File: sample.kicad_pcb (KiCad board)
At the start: 2 copper layers, 35 parts, among them CN10 Conn_02x17_Odd_Even, CN7 Conn_02x10_Odd_Even, CN8 Conn_02x08_Odd_Even, CN9 Conn_02x15_Odd_Even, U1 TJA1042T-3, U2 TJA1042T-3, U3 TJA1042T-3

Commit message: placements
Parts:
- moved U1 1.24 mm to (128.3, 57.7)
- moved U2 0.87 mm to (128.3, 89.7)
- moved CAN1 0.74 mm to (163.3, 53.0)
- moved U3 0.37 mm to (128.3, 117.7)
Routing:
- net CAN1_H: track 0.00 -> 35.1 mm
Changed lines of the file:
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@@
 	(footprint "Package_SO:SOIC-8_3.9x4.9mm_P1.27mm"
 		(layer "F.Cu")
-		(at 127.4 89.74)
+		(at 128.27 89.74)
 		(descr "SOIC, 8 Pin (JEDEC MS-012AA, https://www.analog.com/media/en/package-pcb-resources/package/pkg_pdf/soic_narrow-r/r_8.pdf), generated with kicad-footprint-generator ipc_gullwing_generator.py")
 		(tags "SOIC SO")
@@
 	(footprint "Package_SO:SOIC-8_3.9x4.9mm_P1.27mm"
 		(layer "F.Cu")
-		(at 127.9 117.74)
+		(at 128.27 117.74)
 		(descr "SOIC, 8 Pin (JEDEC MS-012AA, https://www.analog.com/media/en/package-pcb-resources/package/pkg_pdf/soic_narrow-r/r_8.pdf), generated with kicad-footprint-generator ipc_gullwing_generator.py")
 		(tags "SOIC SO")
@@
 	(footprint "Connector_Dsub:DSUB-9_Female_Horizontal_P2.77x2.54mm_EdgePinOffset9.40mm"
 		(layer "F.Cu")
-		(at 163.269669 53.69 90)
+		(at 163.269669 52.95 90)
 		(descr "9-pin D-Sub connector, horizontal/angled (90 deg), THT-mount, female, pitch 2.77x2.54mm, pin-PCB-offset 9.4mm, see http://docs-europe.electrocomponents.com/webdocs/1585/0900766b81585df2.pdf")
 		(tags "9-pin D-Sub connector horizontal angled 90deg THT female pitch 2.77x2.54mm pin-PCB-offset 9.4mm")
@@
 	(footprint "Package_SO:SOIC-8_3.9x4.9mm_P1.27mm"
 		(layer "F.Cu")
-		(at 129.4 58.24)
+		(at 128.27 57.74)
 		(descr "SOIC, 8 Pin (JEDEC MS-012AA, https://www.analog.com/media/en/package-pcb-resources/package/pkg_pdf/soic_narrow-r/r_8.pdf), generated with kicad-footprint-generator ipc_gullwing_generator.py")
 		(tags "SOIC SO")
@@
 	)
 	(gr_line
-		(start 98.9 126.74)
-		(end 178.401667 126.74)
-		(stroke
-			(width 0.1)
-			(type default)
-		)
-		(layer "F.SilkS")
-	)
-	(gr_line
 		(start 103.4 126.74)
 		(end 103.4 94.74)
@@
 		(layer "F.SilkS")
 	)
+	(segment
+		(start 130.745 57.105)
+		(end 165.809669 57.105)
+		(width 0.2)
+		(layer "F.Cu")
+		(net 19)
+	)
 )

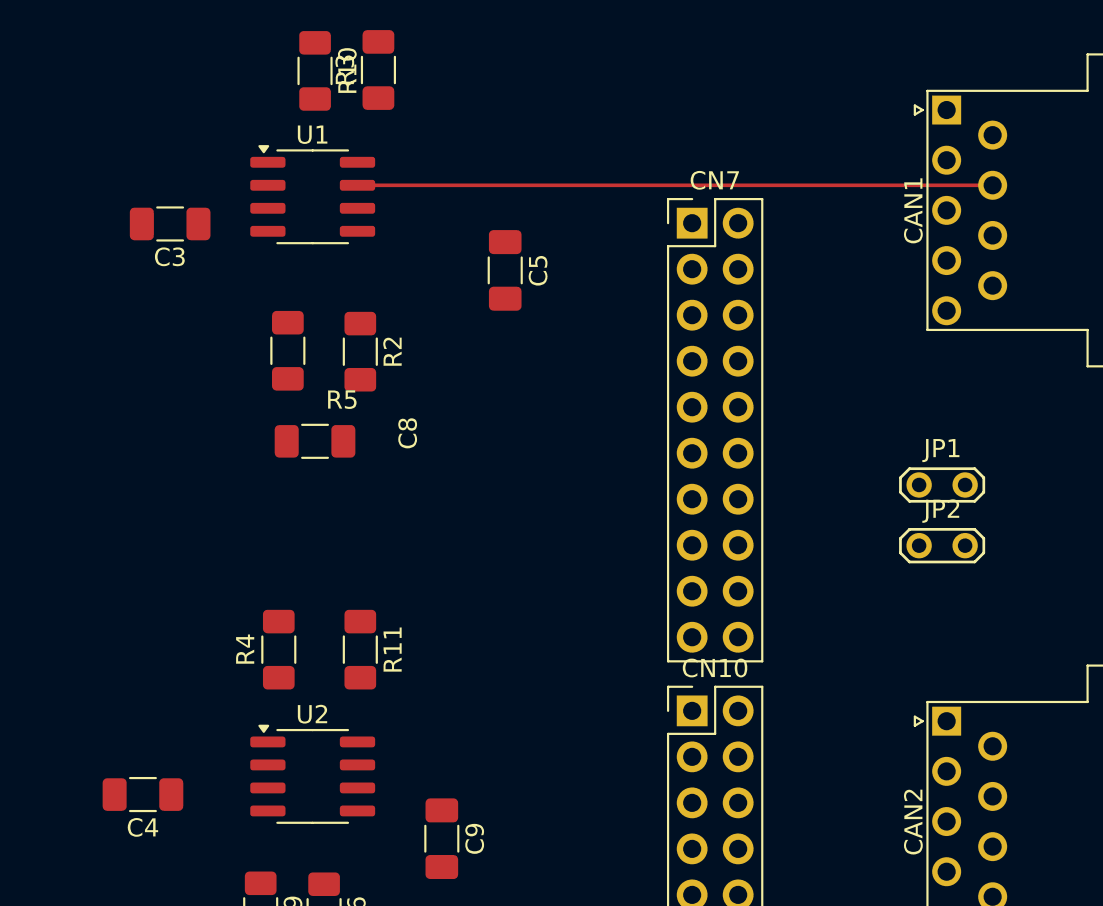
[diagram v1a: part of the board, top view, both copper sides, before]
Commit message: adapt Signal net rule
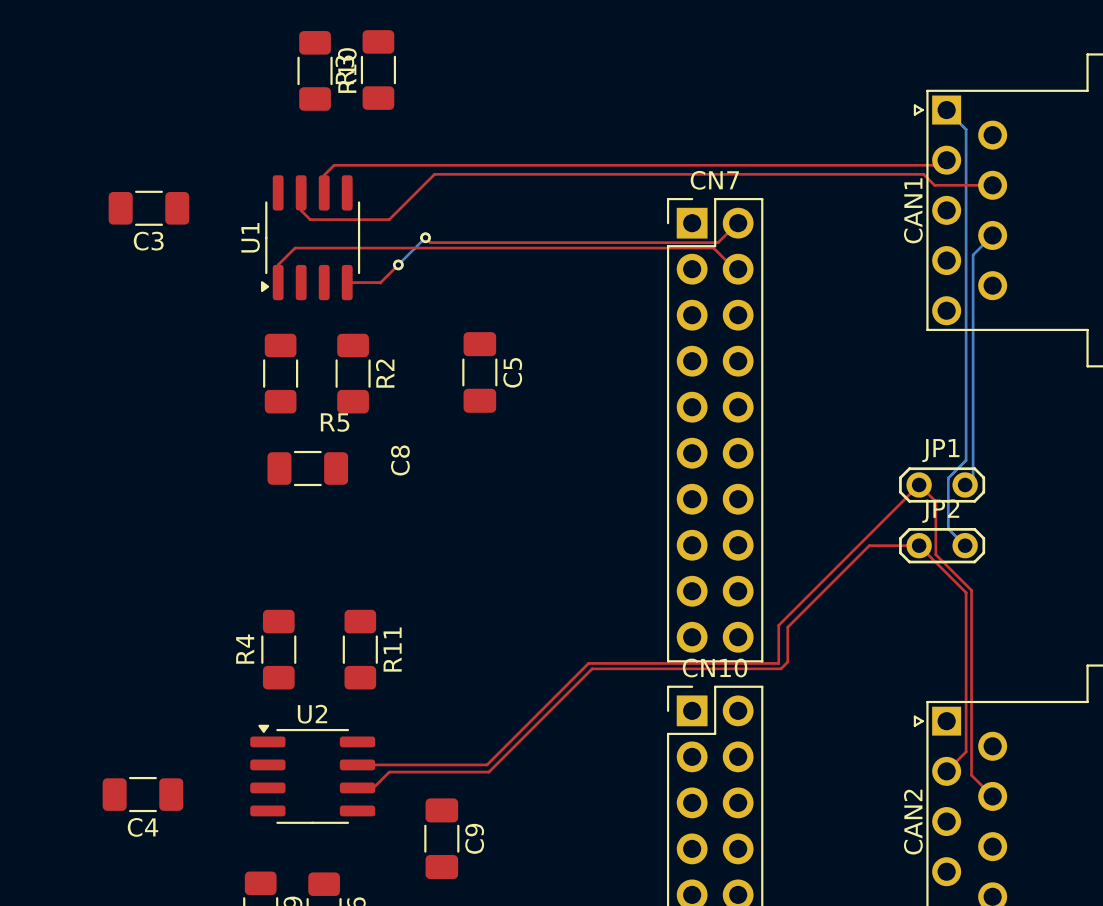
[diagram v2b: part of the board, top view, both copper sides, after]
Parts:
- moved C5 5.81 mm to (137.5, 67.4)
- moved U1 2.26 mm to (128.3, 60.0), turned to 90 degrees
- moved C8 1.55 mm to (128.0, 72.7)
- moved C3 1.45 mm to (119.2, 58.4)
- moved R5 1.32 mm to (126.5, 67.5)
- moved R2 1.27 mm to (130.5, 67.5)
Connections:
- net Net-(JP1-B) renamed CAN2_HR
- net Net-(JP2-B) renamed CAN2_LR
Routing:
- net CAN2_H: track 0.00 -> 57.5 mm
- net CAN2_L: track 0.00 -> 51.7 mm
- net CAN1_L: track 0.00 -> 35.7 mm
- net CAN1_TX: track 0.00 -> 27.0 mm
- net CAN2_LR: track 0.00 -> 25.3 mm
- net CAN1_RX: track 0.00 -> 23.2 mm, vias 0 -> 2
- net CAN2_HR: track 0.00 -> 14.4 mm
- net CAN1_H: track 35.1 -> 40.6 mm

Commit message: uarts routed
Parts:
- moved C2 14.1 mm to (121.5, 123.5)
- moved C1 3.42 mm to (121.0, 115.5)
- moved R12 1.42 mm to (125.0, 109.5)
- moved R1 0.90 mm to (129.5, 109.7)
- turned U3 to -90 degrees
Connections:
- CN10 pad 2: USART10_TX -> /ZIO Connector/PG12
- CN10 pad 25: USART10_RX -> unconnected-(CN10-Pin_25-Pad25)
- CN10 pad 28: /ZIO Connector/PE6 -> unconnected-(CN10-Pin_28-Pad28)
- CN10 pad 29: UART4_TX -> /ZIO Connector/PA0
- CN8 pad 8: UART4_RX -> /ZIO Connector/PC11
- CN9 pad 22: /ZIO Connector/PE3 -> USART10_TX
- CN9 pad 25: /ZIO Connector/PD0 -> UART4_RX
- CN9 pad 27: /ZIO Connector/PD1 -> UART4_TX
- DeviceUART1 pad 1: USART2_TX -> UART7_TX
- DeviceUART1 pad 4: USART6_RX -> UART9_RX
- DeviceUART1 pad 5: USART10_RX -> UART4_RX
- DeviceUART1 pad 6: USART2_RX -> UART7_RX
- DeviceUART1 pad 8: USART6_TX -> UART9_TX
- DeviceUART1 pad 9: USART10_TX -> UART4_TX
- RoutedUART1 pad 1: UART4_RX -> USART6_RX
- RoutedUART1 pad 4: UART7_TX -> USART2_TX
- RoutedUART1 pad 5: UART9_TX -> USART10_TX
- RoutedUART1 pad 6: UART4_TX -> USART6_TX
- RoutedUART1 pad 8: UART7_RX -> USART2_RX
- RoutedUART1 pad 9: UART9_RX -> USART10_RX
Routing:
- net UART7_RX: track 0.00 -> 103.8 mm
- net UART7_TX: track 0.00 -> 102.1 mm
- net USART6_RX: track 0.00 -> 85.5 mm
- net USART3_RX: track 0.00 -> 81.6 mm
- net USART3_TX: track 0.00 -> 78.9 mm
- net USART6_TX: track 0.00 -> 78.1 mm
- net USART10_TX: track 0.00 -> 44.0 mm
- net CAN3_H: track 0.00 -> 40.0 mm
- net CAN3_L: track 0.00 -> 38.9 mm
- net USART10_RX: track 0.00 -> 37.7 mm
- net CAN2_TX: track 0.00 -> 32.7 mm
- net CAN2_RX: track 0.00 -> 30.6 mm, vias 0 -> 2
- net UART9_TX: track 0.00 -> 27.8 mm
- net UART4_TX: track 0.00 -> 27.6 mm
- net USART2_TX: track 0.00 -> 26.2 mm
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
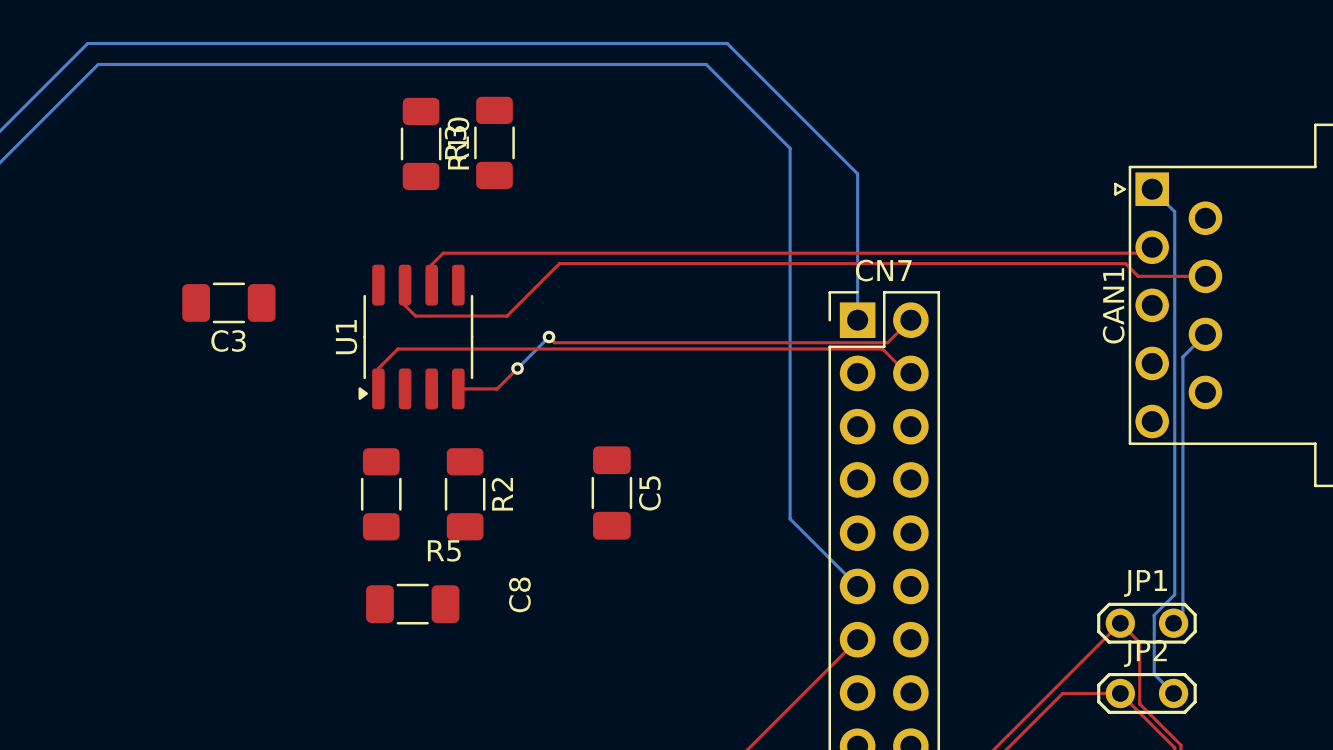
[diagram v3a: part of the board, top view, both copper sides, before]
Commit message: some connection for CAN1
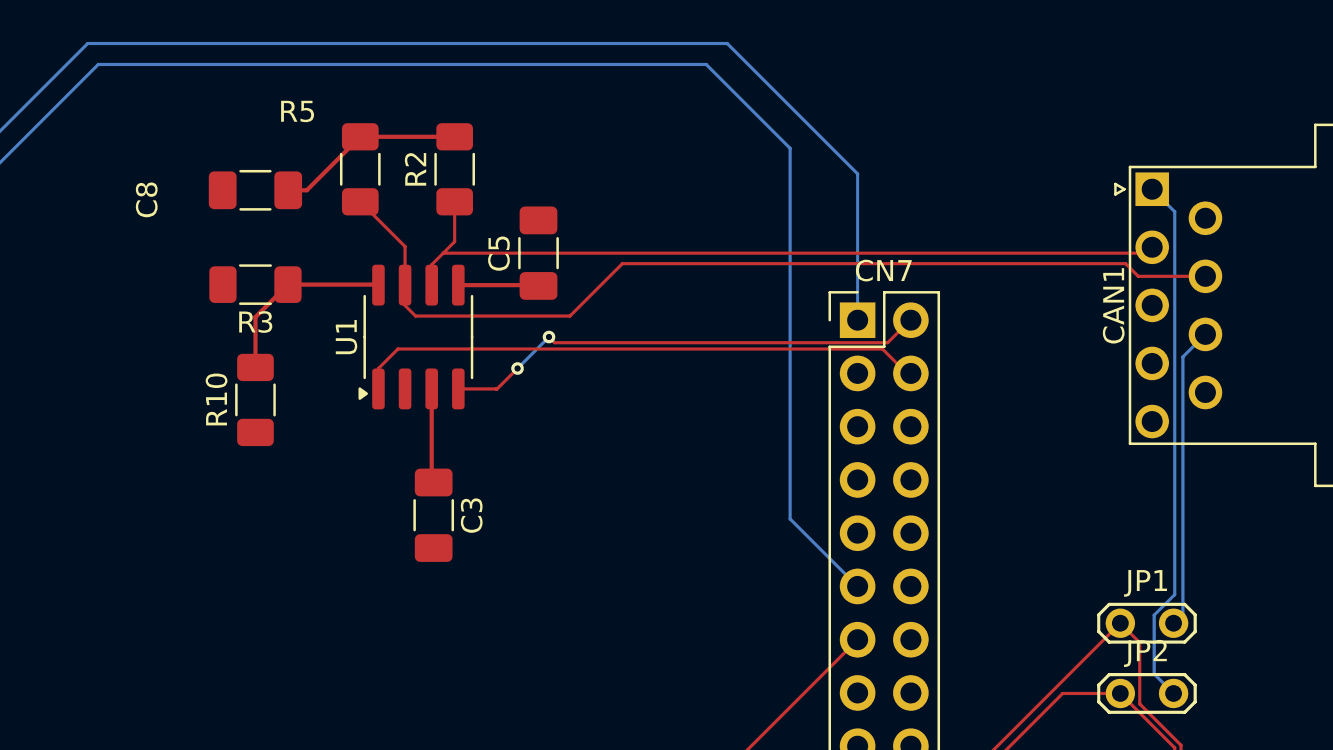
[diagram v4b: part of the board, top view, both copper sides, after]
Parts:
- moved C8 21.1 mm to (120.5, 53.0), turned to 180 degrees
- moved R5 15.5 mm to (125.5, 52.0), turned to 90 degrees
- moved R2 15.5 mm to (130.0, 52.0), turned to 90 degrees
- moved R10 14.5 mm to (120.5, 63.0), turned to 90 degrees
- moved C3 14.1 mm to (129.0, 68.5), turned to -90 degrees
- moved R3 13.3 mm to (120.5, 57.5), turned to 180 degrees
- moved C5 12.0 mm to (134.0, 56.0), turned to 90 degrees
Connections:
- CN7 pad 3: /ZIO Connector/PB15 -> CAN1_STB
- CN7 pad 7: CAN1_STB -> /ZIO Connector/PB12
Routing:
- net Net-(C8-Pad1): track 0.00 -> 8.99 mm
- net Net-(U1-STB): track 0.00 -> 8.92 mm
- net CAN1_H: track 40.6 -> 45.5 mm
- net +5V: track 0.00 -> 4.50 mm
- net +3V3: track 0.00 -> 3.89 mm
- net CAN1_L: track 35.7 -> 38.4 mm

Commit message: CAN1 finished
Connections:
- CN7 pad 14: CAN2_RX -> unconnected-(CN7-Pin_14-Pad14)
- CN7 pad 3: CAN1_STB -> /ZIO Connector/PB15
- CN7 pad 7: /ZIO Connector/PB12 -> CAN1_STB
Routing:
- net CAN1_STB: track 0.00 -> 29.7 mm, vias 0 -> 1
- net USART6_RX: track 85.5 -> 88.0 mm
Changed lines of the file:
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@@
 	(net 122 "unconnected-(CN10-Pin_28-Pad28)")
 	(net 123 "unconnected-(CN10-Pin_25-Pad25)")
-	(net 124 "/ZIO Connector/PB12")
+	(net 124 "/ZIO Connector/PB15")
+	(net 125 "unconnected-(CN7-Pin_14-Pad14)")
 	(footprint "Capacitor_SMD:C_1206_3216Metric_Pad1.33x1.80mm_HandSolder"
 		(layer "F.Cu")
@@
 			(layers "*.Cu" "*.Mask")
 			(remove_unused_layers no)
-			(net 17 "CAN1_STB")
+			(net 124 "/ZIO Connector/PB15")
 			(pinfunction "Pin_3")
 			(pintype "passive")
@@
 			(layers "*.Cu" "*.Mask")
 			(remove_unused_layers no)
-			(net 124 "/ZIO Connector/PB12")
+			(net 17 "CAN1_STB")
 			(pinfunction "Pin_7")
 			(pintype "passive")
@@
 			(layers "*.Cu" "*.Mask")
 			(remove_unused_layers no)
-			(net 25 "CAN2_RX")
+			(net 125 "unconnected-(CN7-Pin_14-Pad14)")
 			(pinfunction "Pin_14")
-			(pintype "passive")
+			(pintype "passive+no_connect")
 		)
 		(pad "15" thru_hole oval
@@
 	)
 	(segment
+		(start 120.5 64.55)
+		(end 122.45 64.55)
+		(width 0.15)
+		(layer "F.Cu")
+		(net 17)
+	)
+	(segment
+		(start 122.45 64.55)
+		(end 122.5 64.5)
+		(width 0.15)
+		(layer "F.Cu")
+		(net 17)
+	)
+	(via
+		(at 122.5 64.5)
+		(size 0.6)
+		(drill 0.3)
+		(layers "F.Cu" "B.Cu")
+		(net 17)
+	)
+	(segment
+		(start 122.5 64.5)
+		(end 146.904 64.5)
+		(width 0.15)
+		(layer "B.Cu")
+		(net 17)
+	)
+	(segment
+		(start 146.904 64.5)
+		(end 149.22 66.816)
+		(width 0.15)
+		(layer "B.Cu")
+		(net 17)
+	)
+	(segment
 		(start 162.605 57.105)
 		(end 165.809669 57.105)
@@
 	)
 	(segment
-		(start 93.930331 66.069669)
-		(end 93.930331 67.69)
+		(start 146.811 62.811)
+		(end 146 62)
 		(width 0.15)
 		(layer "B.Cu")
@@
 	)
 	(segment
-		(start 113 47)
-		(end 93.930331 66.069669)
+		(start 149.27528 62.811)
+		(end 150.5 64.03572)
 		(width 0.15)
 		(layer "B.Cu")
@@
 	)
 	(segment
-		(start 146 51)
-		(end 142 47)
+		(start 113 47)
+		(end 93.930331 66.069669)
 		(width 0.15)
 		(layer "B.Cu")
@@
 	(segment
 		(start 149.22 71.896)
-		(end 146 68.676)
+		(end 150.5 70.616)
 		(width 0.15)
 		(layer "B.Cu")
@@
 	)
 	(segment
-		(start 146 68.676)
+		(start 146 62)
 		(end 146 51)
 		(width 0.15)
@@
 	)
 	(segment
+		(start 146.811 62.811)
+		(end 149.27528 62.811)
+		(width 0.15)
+		(layer "B.Cu")
+		(net 98)
+	)
+	(segment
+		(start 93.930331 66.069669)
+		(end 93.930331 67.69)
+		(width 0.15)
+		(layer "B.Cu")
+		(net 98)
+	)
+	(segment
+		(start 150.5 70.616)
+		(end 150.5 64.03572)
+		(width 0.15)
+		(layer "B.Cu")
+		(net 98)
+	)
+	(segment
 		(start 142 47)
 		(end 113 47)
 		(width 0.15)
 		(layer "B.Cu")
+		(net 98)
+	)
+	(segment
+		(start 146 51)
+		(end 142 47)
+		(width 0.15)
+		(layer "B.Cu")

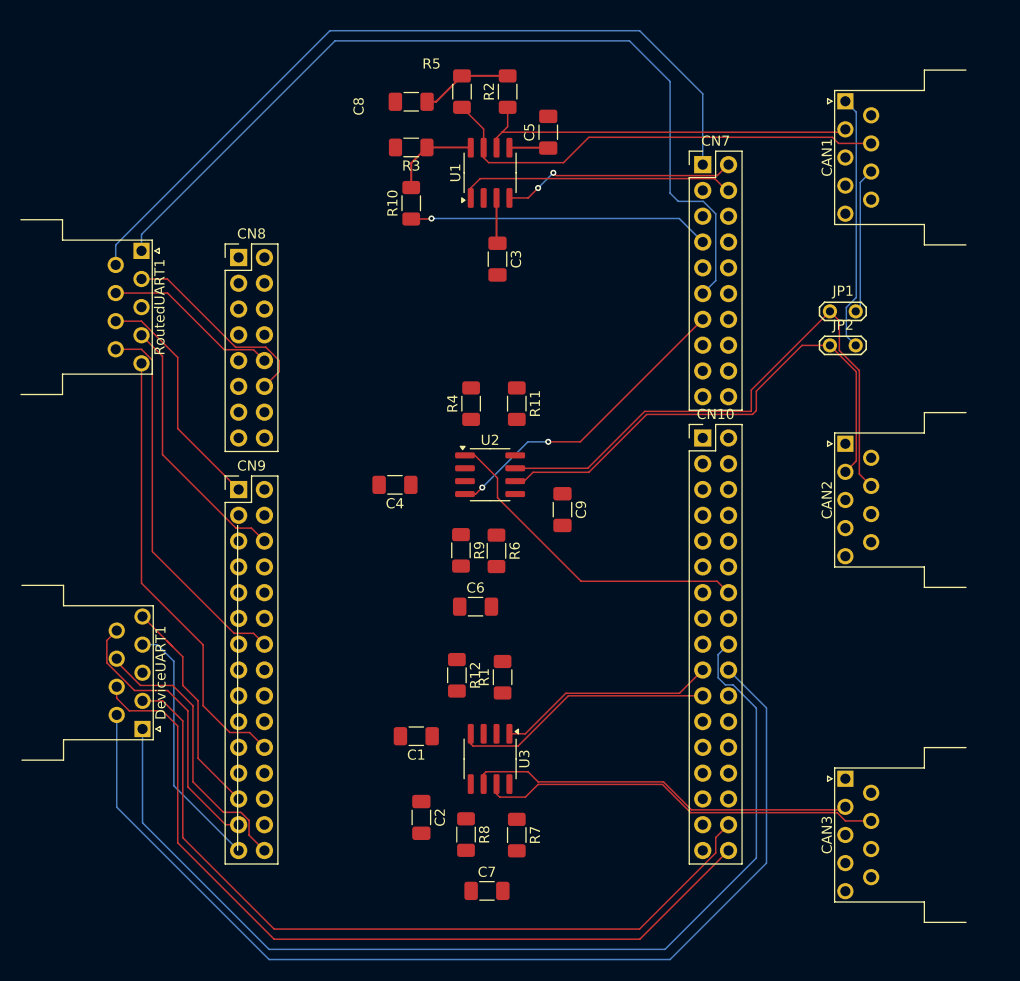
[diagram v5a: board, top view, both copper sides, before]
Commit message: All nets conected except GND, +3V3, +5V
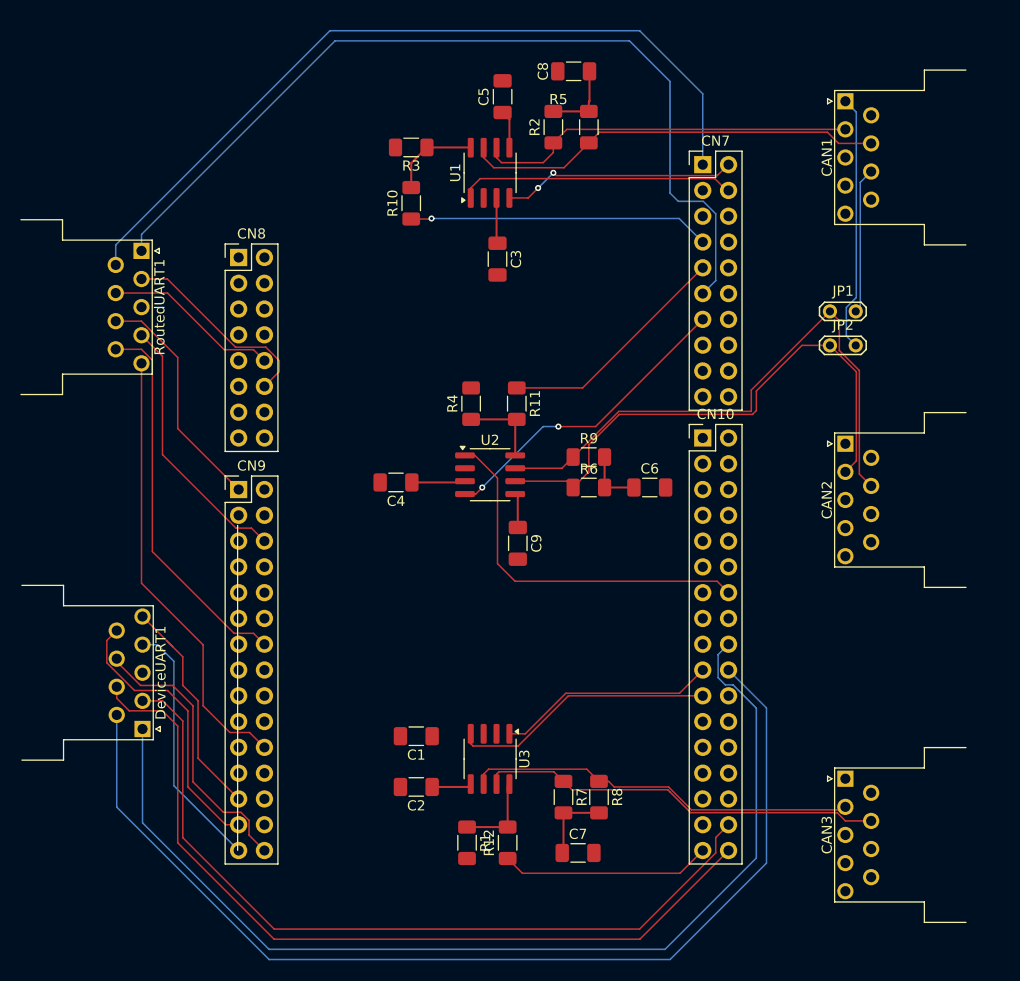
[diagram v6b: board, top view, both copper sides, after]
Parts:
- moved C6 20.8 mm to (144.0, 91.0)
- moved R12 17.2 mm to (130.0, 126.0), turned to 90 degrees
- moved R1 16.7 mm to (126.0, 126.0), turned to -90 degrees
- moved C8 16.3 mm to (136.5, 50.0)
- moved R9 15.6 mm to (138.0, 88.0), turned to 0 degrees
- moved R8 13.6 mm to (139.0, 121.5)
- moved R5 13.0 mm to (138.0, 55.5)
- moved R6 11.0 mm to (138.0, 91.0), turned to 0 degrees
- moved C7 9.72 mm to (136.9, 127.0)
- moved R7 5.93 mm to (135.5, 121.5)
- moved C5 5.70 mm to (129.5, 52.5)
- moved R2 5.70 mm to (134.5, 55.5)
- moved C9 5.51 mm to (131.0, 96.5)
- moved C2 3.04 mm to (121.0, 120.5), turned to 180 degrees
- moved C4 0.26 mm to (119.0, 90.5)
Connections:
- CN10 pad 15: CAN2_STB -> /ZIO Connector/PB2
- CN10 pad 23: CAN3_STB -> /ZIO Connector/PD11
- CN10 pad 33: /ZIO Connector/PE0 -> CAN3_STB
- CN7 pad 9: /ZIO Connector/PA15 -> CAN2_STB
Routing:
- net CAN2_STB: track 0.00 -> 23.2 mm
- net CAN3_STB: track 0.00 -> 20.7 mm
- net Net-(U3-STB): track 0.00 -> 8.31 mm
- net Net-(U2-STB): track 0.00 -> 8.11 mm
- net Net-(C7-Pad1): track 0.00 -> 7.50 mm
- net +3V3: track 3.89 -> 11.1 mm
- net Net-(C6-Pad1): track 0.00 -> 5.89 mm
- net +5V: track 4.50 -> 9.79 mm
- net CAN1_H: track 45.5 -> 41.5 mm
- net CAN2_TX: track 32.7 -> 36.5 mm
- net CAN2_L: track 51.7 -> 53.7 mm
- net Net-(C8-Pad1): track 8.99 -> 7.48 mm
- net CAN1_L: track 38.4 -> 37.5 mm
